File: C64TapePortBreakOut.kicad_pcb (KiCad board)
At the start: 2 copper layers, 26.9 x 26 mm, 6 parts, among them J1 C64-CassettePort, J2 Conn_01x06, J3 Conn_01x02, J4 SCREW_HOLE_1, J5 SCREW_HOLE_2

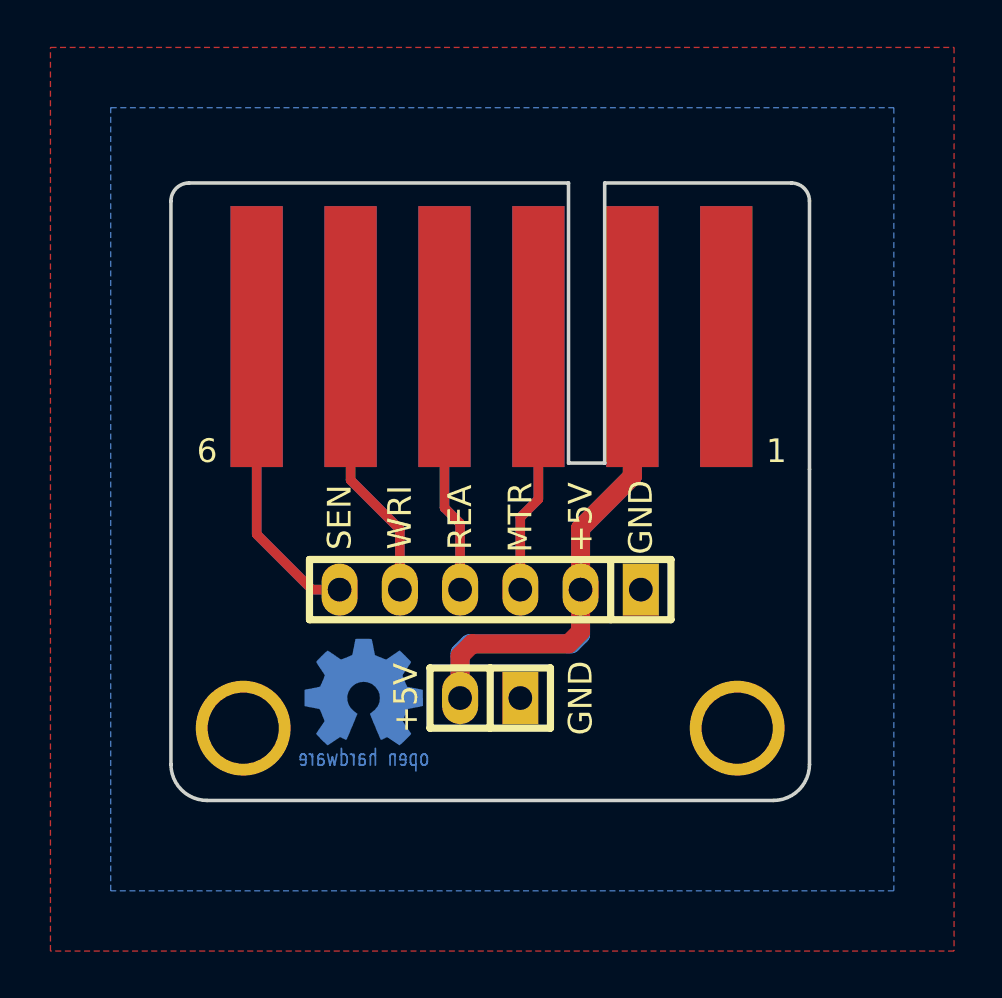
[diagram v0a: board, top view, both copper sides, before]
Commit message: Remove ground plane and solder mask from edge connector
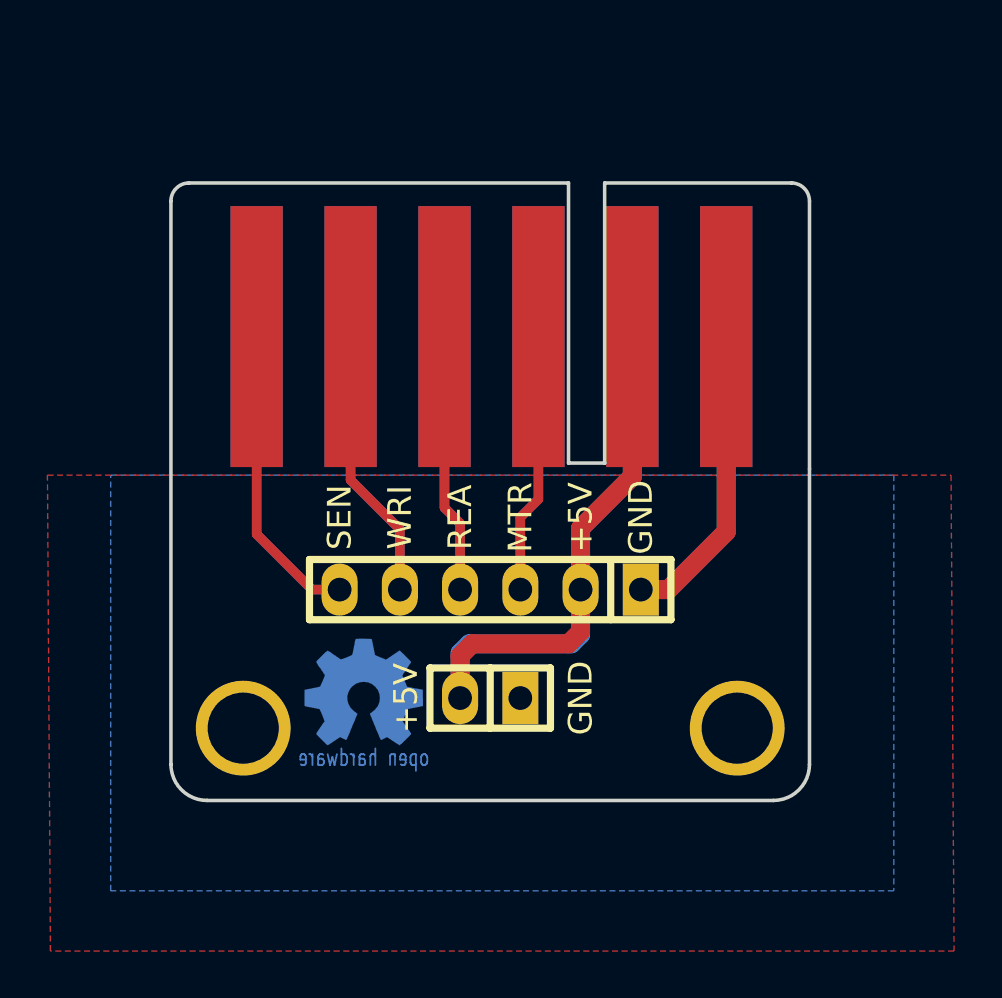
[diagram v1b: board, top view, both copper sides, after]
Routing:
- net Net-(J1-Pad1): track 0.00 -> 25.7 mm
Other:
- board text added: "V2"
- board text removed: "V1"
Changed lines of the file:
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@@
     (links 14)
     (no_connects 0)
-    (area 132.08 79.976449 175.49 119.380001)
+    (area 137.084999 86.919999 164.159001 113.105001)
     (thickness 1.6)
     (drawings 27)
-    (tracks 41)
+    (tracks 49)
     (zones 0)
     (modules 6)
@@
   (title_block
     (title OpenC64TapePortBreakOut)
-    (date 2018-01-08)
-    (rev 1)
+    (date 2018-02-18)
+    (rev 2)
     (company SukkoPera)
   )
@@
   )
   (dimension 26.035 (width 0.3) (layer F.Fab)
-    (gr_text "26,035 mm" (at 168.99 100.0125 270) (layer F.Fab)
+    (gr_text "26,035 mm" (at 174.07 100.0125 270) (layer F.Fab)
       (effects (font (size 1.5 1.5) (thickness 0.3)))
     )
-    (feature1 (pts (xy 164.084 113.03) (xy 170.34 113.03)))
-    (feature2 (pts (xy 164.084 86.995) (xy 170.34 86.995)))
-    (crossbar (pts (xy 167.64 86.995) (xy 167.64 113.03)))
-    (arrow1a (pts (xy 167.64 113.03) (xy 167.053579 111.903496)))
-    (arrow1b (pts (xy 167.64 113.03) (xy 168.226421 111.903496)))
-    (arrow2a (pts (xy 167.64 86.995) (xy 167.053579 88.121504)))
-    (arrow2b (pts (xy 167.64 86.995) (xy 168.226421 88.121504)))
+    (feature1 (pts (xy 164.084 113.03) (xy 175.42 113.03)))
+    (feature2 (pts (xy 164.084 86.995) (xy 175.42 86.995)))
+    (crossbar (pts (xy 172.72 86.995) (xy 172.72 113.03)))
+    (arrow1a (pts (xy 172.72 113.03) (xy 172.133579 111.903496)))
+    (arrow1b (pts (xy 172.72 113.03) (xy 173.306421 111.903496)))
+    (arrow2a (pts (xy 172.72 86.995) (xy 172.133579 88.121504)))
+    (arrow2b (pts (xy 172.72 86.995) (xy 173.306421 88.121504)))
   )
   (dimension 26.924 (width 0.3) (layer F.Fab)
@@
     (arrow2b (pts (xy 164.084 82.676449) (xy 162.957496 83.26287)))
   )
-  (gr_text "github.com/SukkoPera/\nOpenC64TapePortBreakOut" (at 150.622 100.965) (layer B.SilkS)
+  (gr_text "github.com/SukkoPera/\nOpenC64TapePortBreakOut" (at 150.622 101.092) (layer B.SilkS)
     (effects (font (size 0.8 0.8) (thickness 0.12)) (justify mirror))
   )
-  (gr_text V1 (at 140.208 106.68) (layer B.SilkS)
+  (gr_text V2 (at 140.208 106.68) (layer B.SilkS)
     (effects (font (size 1 1) (thickness 0.15)) (justify mirror))
   )
-  (gr_text 6 (at 138.684 98.298) (layer F.SilkS)
-    (effects (font (size 1 1) (thickness 0.15)))
-  )
-  (gr_text 1 (at 162.687 98.298) (layer F.SilkS)
-    (effects (font (size 1 1) (thickness 0.15)))
+  (gr_text 6 (at 140.7795 99.949) (layer B.SilkS)
+    (effects (font (size 1 1) (thickness 0.15)) (justify mirror))
+  )
+  (gr_text 1 (at 160.5915 99.949) (layer B.SilkS)
+    (effects (font (size 1 1) (thickness 0.15)) (justify mirror))
   )
   (gr_text +5V (at 147.066 108.712 90) (layer F.SilkS)
@@
   (gr_line (start 162.56 113.03) (end 138.684 113.03) (layer Edge.Cuts) (width 0.15))
   (gr_line (start 164.084 99.06) (end 164.084 111.506) (layer Edge.Cuts) (width 0.15))
+  (segment (start 156.972 104.14) (end 158.134 104.14) (width 0.8) (layer B.Cu) (net 1))
+  (segment (start 158.134 104.14) (end 160.574 101.7) (width 0.8) (layer B.Cu) (net 1))
+  (segment (start 160.574 101.7) (end 160.574 99.372) (width 0.8) (layer B.Cu) (net 1))
+  (segment (start 160.574 99.372) (end 160.574 93.472) (width 0.8) (layer B.Cu) (net 1))
+  (segment (start 156.972 104.14) (end 158.134 104.14) (width 0.8) (layer F.Cu) (net 1))
+  (segment (start 160.574 99.372) (end 160.574 93.472) (width 0.8) (layer F.Cu) (net 1))
+  (segment (start 160.574 101.7) (end 160.574 99.372) (width 0.8) (layer F.Cu) (net 1))
+  (segment (start 158.134 104.14) (end 160.574 101.7) (width 0.8) (layer F.Cu) (net 1))
   (segment (start 154.432 104.14) (end 154.432 106.03982) (width 0.8) (layer B.Cu) (net 2))
   (segment (start 154.432 106.03982) (end 154.04582 106.426) (width 0.8) (layer B.Cu) (net 2))
@@
     (polygon
       (pts
-        (xy 134.62 83.82) (xy 167.64 83.82) (xy 167.64 116.84) (xy 134.62 116.84)
+        (xy 134.62 99.314) (xy 167.64 99.314) (xy 167.64 116.84) (xy 134.62 116.84)
       )
     )
@@
     (polygon
       (pts
-        (xy 132.08 81.28) (xy 170.18 81.28) (xy 170.18 119.38) (xy 132.08 119.38)
+        (xy 131.953 99.314) (xy 170.053 99.314) (xy 170.18 119.38) (xy 132.08 119.38)
       )
     )
+  )
+  (zone (net 0) (net_name "") (layer F.Mask) (hatch edge 0.508)
+    (connect_pads (clearance 0.1))
+    (min_thickness 0.254)
+    (fill yes (arc_segments 16) (thermal_gap 0.508) (thermal_bridge_width 0.508))
+    (polygon
+      (pts
+        (xy 132.08 86.36) (xy 170.18 86.36) (xy 170.307 98.933) (xy 132.207 98.933)
+      )
+    )
+  )
+  (zone (net 0) (net_name "") (layer B.Mask) (hatch edge 0.508)
+    (connect_pads (clearance 0.1))
+    (min_thickness 0.254)
+    (fill yes (arc_segments 16) (thermal_gap 0.508) (thermal_bridge_width 0.508))
+    (polygon
+      (pts
+        (xy 167.64 98.933) (xy 167.64 86.36) (xy 134.62 86.36) (xy 134.62 98.933)
+      )
+    )
